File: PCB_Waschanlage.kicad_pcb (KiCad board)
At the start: 2 copper layers, 228 x 75 mm, 82 parts, among them J1 DSUB_1, J10 JMPR_LED_BTN_Sensor_1, J11 JMPR_LED_BTN_Sensor_4, J12 Conn_LED_Error, J13 Conn_LED_MainWash, J14 Conn_BTN_Start, J15 Conn_BTN_Basic, J16 Conn_LED_Motor, J17 Conn_LED_Red, J18 Conn_BTN_Sensor_1, J19 Conn_BTN_Sensor_4, J2 DSUB_2, J20 JMPR_LED_PreWash, J21 JMPR_LED_Start, J22 JMPR_LED_Basic, J23 JMPR_LED_BTN_On_Off, J24 JMPR_LED_BTN_Special, J25 JMPR_LED_Green, J26 JMPR_LED_BTN_Sensor_2, J27 JMPR_LED_BTN_Sensor_5, J28 Conn_LED_PreWash, J29 Conn_LED_Start, J3 Conn_Fuse, J30 Conn_LED_Basic, J31 Conn_BTN_On_Off, J32 Conn_BTN_Special, J33 Conn_LED_Green, J34 Conn_BTN_Sensor_2, J35 Conn_BTN_Sensor_5, J36 JMPR_LED_Special, J37 JMPR_LED_Care, J38 JMPR_LED_Underbody, J39 JMPR_LED_BTN_EmergencyOff, J4 JMPR_LED_Error, J40 JMPR_LED_BTN_Premium, J41 JMPR_LED_BTN_Sensor_3, J42 Conn_LED_Special, J43 Conn_LED_Care, J44 Conn_LED_Underbody, J45 Conn_BTN_EmergencyOff, J46 Conn_BTN_Premium, J47 Conn_BTN_Sensor_3, J48 JMPR_LED_Rims, J49 JMPR_LED_Premium, J5 JMPR_LED_MainWash, J50 JMPR_LED_Dry, J51 Conn_LED_Rims, J52 Conn_LED_Premium, J53 Conn_LED_Dry, J54 Conn_AdditionalPins_1, J55 Conn_AdditionalPins_2, J56 Conn_AdditionalPins_3, J6 JMPR_LED_BTN_Start, J7 JMPR_LED_BTN_Basic, J8 JMPR_LED_Motor, J9 JMPR_LED_Red

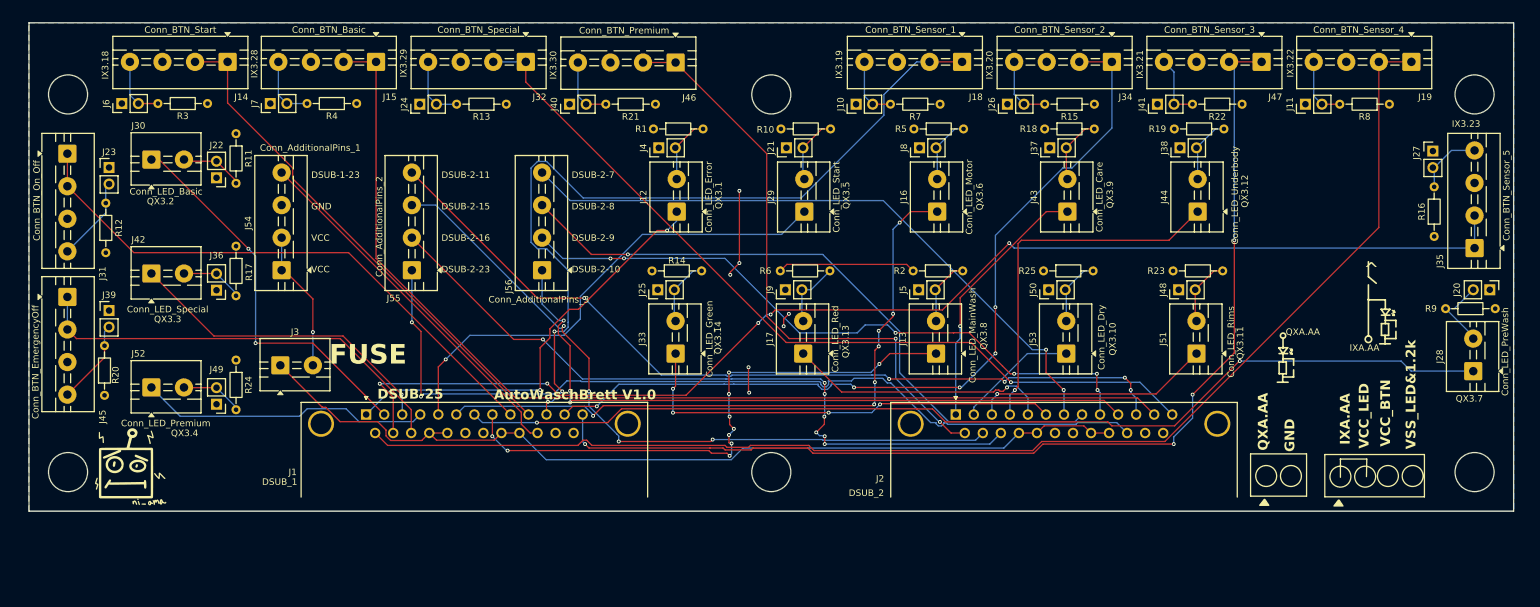
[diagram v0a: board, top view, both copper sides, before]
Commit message: Changed Connectors and Rerouting
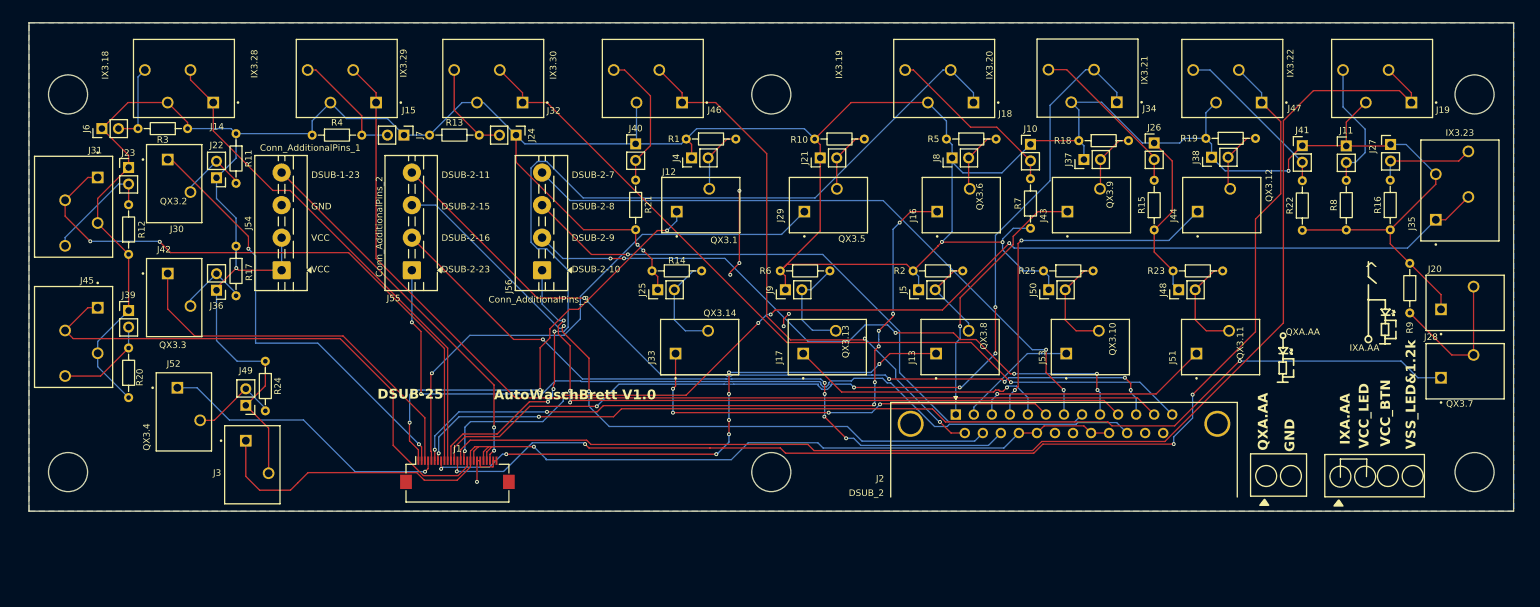
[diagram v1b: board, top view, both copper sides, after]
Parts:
- removed G***: LOGO, Doodles:robot
- J1: footprint Connector_Dsub:DSUB-25_Pins_Horizontal_P2.77x2.84mm_EdgePinOffset9.90mm_Housed_MountingHolesOffset11.32mm -> Connector_FFC-FPC:Hirose_FH12-25S-0.5SH_1x25-1MP_P0.50mm_Horizontal
- J12, J13, J16, J17, J28, J29, J3, J30, J33, J42, J43, J44, J51, J52, J53: footprint TerminalBlock:TerminalBlock_MaiXu_MX126-5.0-02P_1x02_P5.00mm -> TBL002A-350-02GY-2GY:CUI_TBL002A-350-02GY-2GY
- J14, J15, J18, J19, J31, J32, J34, J35, J45, J46, J47: footprint TerminalBlock:TerminalBlock_MaiXu_MX126-5.0-04P_1x04_P5.00mm -> TBL002A-350-04GY-2GY:CUI_TBL002A-350-04GY-2GY
- J20: footprint Connector_PinHeader_2.54mm:PinHeader_1x02_P2.54mm_Vertical -> TBL002A-350-02GY-2GY:CUI_TBL002A-350-02GY-2GY
- moved J10 27.5 mm to (194.5, 77.7), turned to 0 degrees
- moved R7 23.6 mm to (194.5, 90.6), turned to 90 degrees
- moved J26 23.3 mm to (213.5, 77.5), turned to 0 degrees
- moved J41 23.1 mm to (236.2, 77.9), turned to 0 degrees
- moved R22 21.5 mm to (236.2, 90.9), turned to 90 degrees
- moved R15 21.4 mm to (213.5, 90.8), turned to 90 degrees
- moved J7 21.1 mm to (98.3, 76.2), turned to -90 degrees
- moved R8 20.4 mm to (243.0, 90.8), turned to 90 degrees
- moved R21 19.5 mm to (133.9, 90.8), turned to 90 degrees
- moved J1 16.6 mm to (106.5, 128.1)
- moved J24 15.5 mm to (115.5, 76.2), turned to -90 degrees
- moved R9 14.9 mm to (252.8, 95.9), turned to -90 degrees
- moved J3 12.7 mm to (74.0, 123.2)
- moved R13 12.7 mm to (102.2, 76.2), turned to 0 degrees
- moved J40 11.8 mm to (133.9, 77.6), turned to 0 degrees
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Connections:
- J10 pad 1: GND -> VCC
- J11 pad 1: GND -> VCC
- J14 pad 3: GND -> VCC
- J15 pad 3: GND -> VCC
- J18 pad 3: GND -> VCC
- J19 pad 3: GND -> VCC
- J20 pad 1: GND -> VCC
- J21 pad 1: GND -> VCC
- J22 pad 1: GND -> VCC
- J23 pad 1: GND -> VCC
- J24 pad 1: GND -> VCC
- J25 pad 1: GND -> VCC
- J26 pad 1: GND -> VCC
- J27 pad 1: GND -> VCC
- J31 pad 3: GND -> VCC
- J32 pad 3: GND -> VCC
- J34 pad 3: GND -> VCC
- J35 pad 3: GND -> VCC
- J36 pad 1: GND -> VCC
- J37 pad 1: GND -> VCC
- J38 pad 1: GND -> VCC
- J39 pad 1: GND -> VCC
- J4 pad 1: GND -> VCC
- J40 pad 1: GND -> VCC
- J41 pad 1: GND -> VCC
- J45 pad 3: GND -> VCC
- J46 pad 3: GND -> VCC
- J47 pad 3: GND -> VCC
- J48 pad 1: GND -> VCC
- J49 pad 1: GND -> VCC
- J5 pad 1: GND -> VCC
- J50 pad 1: GND -> VCC
- J6 pad 1: GND -> VCC
- J7 pad 1: GND -> VCC
- J8 pad 1: GND -> VCC
- J9 pad 1: GND -> VCC
- R1 pad 1: GND -> VCC
- R10 pad 1: GND -> VCC
- R11 pad 1: GND -> VCC
- R12 pad 1: GND -> VCC
- R13 pad 1: GND -> VCC
- R14 pad 1: GND -> VCC
- R15 pad 1: GND -> VCC
- R16 pad 1: GND -> VCC
- R17 pad 1: GND -> VCC
- R18 pad 1: GND -> VCC
- R19 pad 1: GND -> VCC
- R2 pad 1: GND -> VCC
- R20 pad 1: GND -> VCC
- R21 pad 1: GND -> VCC
- R22 pad 1: GND -> VCC
- R23 pad 1: GND -> VCC
- R24 pad 1: GND -> VCC
- R25 pad 1: GND -> VCC
- R3 pad 1: GND -> VCC
- R4 pad 1: GND -> VCC
- R5 pad 1: GND -> VCC
- R6 pad 1: GND -> VCC
- R7 pad 1: GND -> VCC
- R8 pad 1: GND -> VCC
- R9 pad 1: GND -> VCC
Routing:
- net VCC: track 21.8 -> 607.8 mm, vias 1 -> 6
- net BTN_Sensor_2: track 129.4 -> 149.5 mm
- net BTN_Sensor_1: track 124.1 -> 143.0 mm
- net Net-(J10-Pin_2): track 9.76 -> 27.8 mm
- net BTN_Sensor_3: track 164.4 -> 181.8 mm
- net BTN_EmergencyOff: track 66.5 -> 83.7 mm
- net GND: track 41.1 -> 24.0 mm, vias 7 -> 6
- net BTN_Sensor_5: track 192.3 -> 175.4 mm
- net Net-(J41-Pin_2): track 9.98 -> 25.5 mm
- net Net-(J26-Pin_2): track 10.3 -> 25.4 mm
- net VCC_in: track 140.7 -> 155.7 mm, vias 0 -> 1
- net Net-(J20-Pin_2): track 11.8 -> 23.1 mm
- net Net-(J40-Pin_2): track 9.95 -> 21.2 mm
- net Net-(J11-Pin_2): track 9.76 -> 20.4 mm
- net LED_Special: track 49.2 -> 58.5 mm, vias 1 -> 0
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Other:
- board text removed: "FUSE"

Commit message: Added new connectors on the PCB
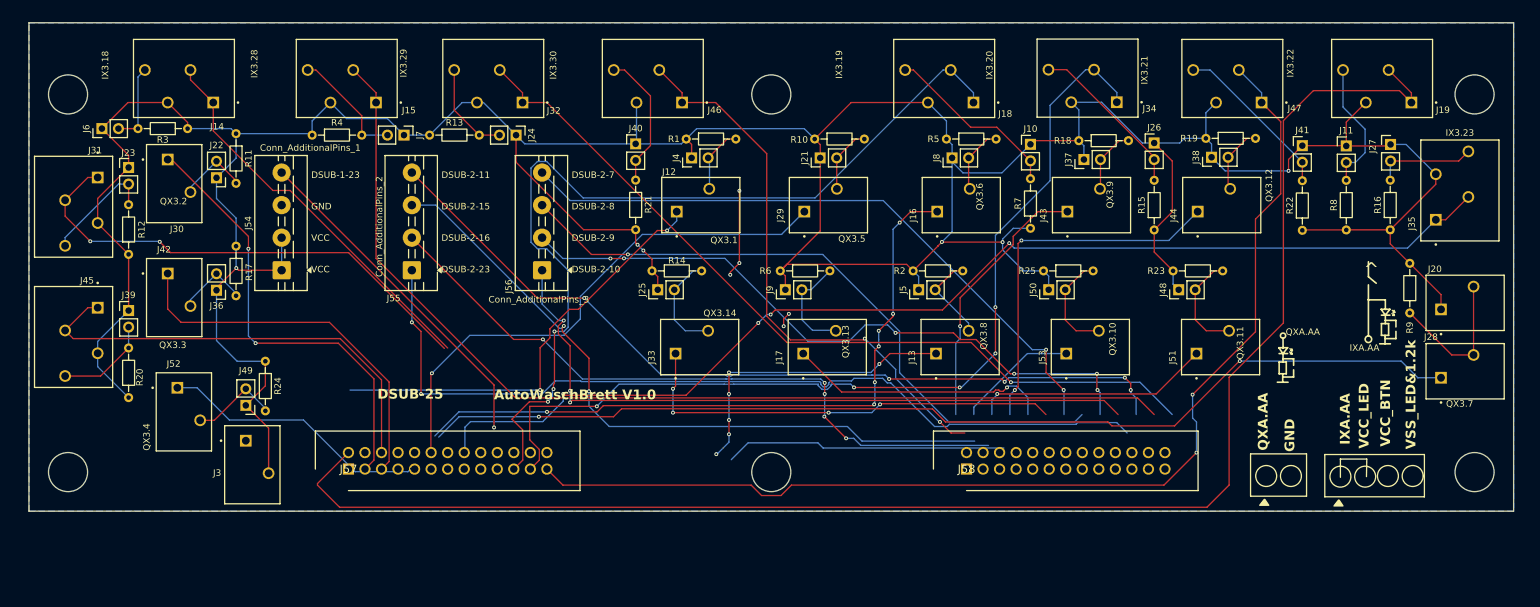
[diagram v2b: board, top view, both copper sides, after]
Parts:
- removed J1: DSUB_1, Connector_FFC-FPC:Hirose_FH12-25S-0.5SH_1x25-1MP_P0.50mm_Horizontal
- removed J2: DSUB_2, Connector_Dsub:DSUB-25_Pins_Horizontal_P2.77x2.84mm_EdgePinOffset9.90mm_Housed_MountingHolesOffset11.32mm
- added J57: 5103308-6, project:SHDR26W66P254_2X13_4051X914X986P, F.Cu at (89.8, 127.5)
- added J58: 5103308-6, project:SHDR26W66P254_2X13_4051X914X986P, F.Cu at (184.7, 127.5)
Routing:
- net VCC_in: track 155.7 -> 43.3 mm, vias 1 -> 0
- net LED_MainWash: track 90.9 -> 46.5 mm, vias 8 -> 6
- net BTN_Sensor_4: track 197.3 -> 238.0 mm
- net BTN_Start: track 77.9 -> 60.6 mm
- net BTN_ON_OFF: track 92.8 -> 75.6 mm
- net BTN_EmergencyOff: track 83.7 -> 69.3 mm
- net BTN_Sensor_3: track 181.8 -> 171.5 mm, vias 4 -> 2
- net GND: track 24.0 -> 15.9 mm, vias 6 -> 5
- net BTN_Sensor_2: track 149.5 -> 144.1 mm
- net DSUB_1_PIN_23: track 58.1 -> 52.7 mm, vias 2 -> 1
- net BTN_Sensor_1: track 143.0 -> 138.6 mm
- net LED_Premium: track 45.3 -> 41.4 mm
- net LED_Motor: track 109.3 -> 105.5 mm, vias 8 -> 7
- net LED_PreWash: track 165.7 -> 162.0 mm, vias 3 -> 2
- net DSUB_2_PIN_16: track 107.6 -> 104.9 mm
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
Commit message: Routing fimished
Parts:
- J54, J55, J56: footprint TerminalBlock:TerminalBlock_MaiXu_MX126-5.0-04P_1x04_P5.00mm -> TBL002A-350-04GY-2GY:CUI_TBL002A-350-04GY-2GY
- moved J54 13.3 mm to (92.1, 92.6), turned to 180 degrees
- moved J55 11.3 mm to (109.9, 92.6), turned to 180 degrees
- moved J56 9.31 mm to (127.7, 92.6), turned to 180 degrees
- moved J3 5.89 mm to (72.2, 117.5)
- moved J49 5.39 mm to (72.0, 112.8)
- moved R24 5.01 mm to (75.5, 106.2)
- moved J58 3.02 mm to (184.3, 124.5)
- moved J57 3.00 mm to (89.8, 124.5)
- moved J52 2.50 mm to (62.5, 112.8)
- moved J40 2.40 mm to (136.0, 76.5)
- moved R14 1.79 mm to (134.6, 97.2)
- moved J25 1.79 mm to (135.5, 100.1)
- moved R21 1.13 mm to (135.0, 90.8)
- moved R15 0.75 mm to (214.2, 90.8)
- moved J10 0.54 mm to (194.0, 77.5)
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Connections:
- J55 pad 4: DSUB_2_PIN_11 -> DSUB_2_PIN_10
- J56 pad 1: DSUB_2_PIN_10 -> DSUB_2_PIN_11
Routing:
- net VCC_in: track 43.3 -> 220.8 mm, vias 0 -> 2
- net GND: track 15.9 -> 114.0 mm, vias 5 -> 26
- net VCC: track 607.8 -> 691.8 mm, vias 6 -> 0
- net BTN_Sensor_5: track 174.1 -> 244.6 mm, vias 5 -> 1
- net LED_Care: track 40.9 -> 96.6 mm, vias 1 -> 2
- net LED_Basic: track 69.5 -> 119.1 mm, vias 2 -> 0
- net LED_MainWash: track 46.5 -> 92.6 mm, vias 6 -> 1
- net BTN_Sensor_2: track 144.1 -> 189.7 mm, vias 5 -> 0
- net DSUB_2_PIN_9: track 102.4 -> 135.9 mm, vias 6 -> 2
- net DSUB_2_PIN_10: track 108.4 -> 139.2 mm, vias 3 -> 0
- net LED_Underbody: track 56.4 -> 78.9 mm, vias 2 -> 1
- net BTN_Basic: track 159.8 -> 182.0 mm
- net BTN_Start: track 60.6 -> 81.8 mm
- net DSUB_2_PIN_7: track 99.8 -> 120.9 mm, vias 2 -> 1
- net BTN_Sensor_4: track 238.0 -> 258.7 mm
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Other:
- board text added: "DSUB-1-23"
- board text added: "DSUB-2-10"
- board text added: "DSUB-2-11"
- board text added: "DSUB-2-15"
- board text added: "DSUB-2-16"
- board text added: "DSUB-2-23"
- board text added: "DSUB-2-7"
- board text added: "DSUB-2-8"
- board text added: "DSUB-2-9"
- board text added: "LED ???"
- board text added: "LED motor"
- board text added: "LED start"
- board text added: "Spare I/O"
- board text added: "VCC"
- board text added: "basic button"
- board text added: "premium button"
- board text added: "special button"
- board text added: "start button"
- board text removed: "DSUB-1-23 GND VCC VCC"
- board text removed: "DSUB-2-11 DSUB-2-15 DSUB-2-16 DSUB-2-23"
- board text removed: "DSUB-2-7 DSUB-2-8 DSUB-2-9 DSUB-2-10"
- board text removed: "^"

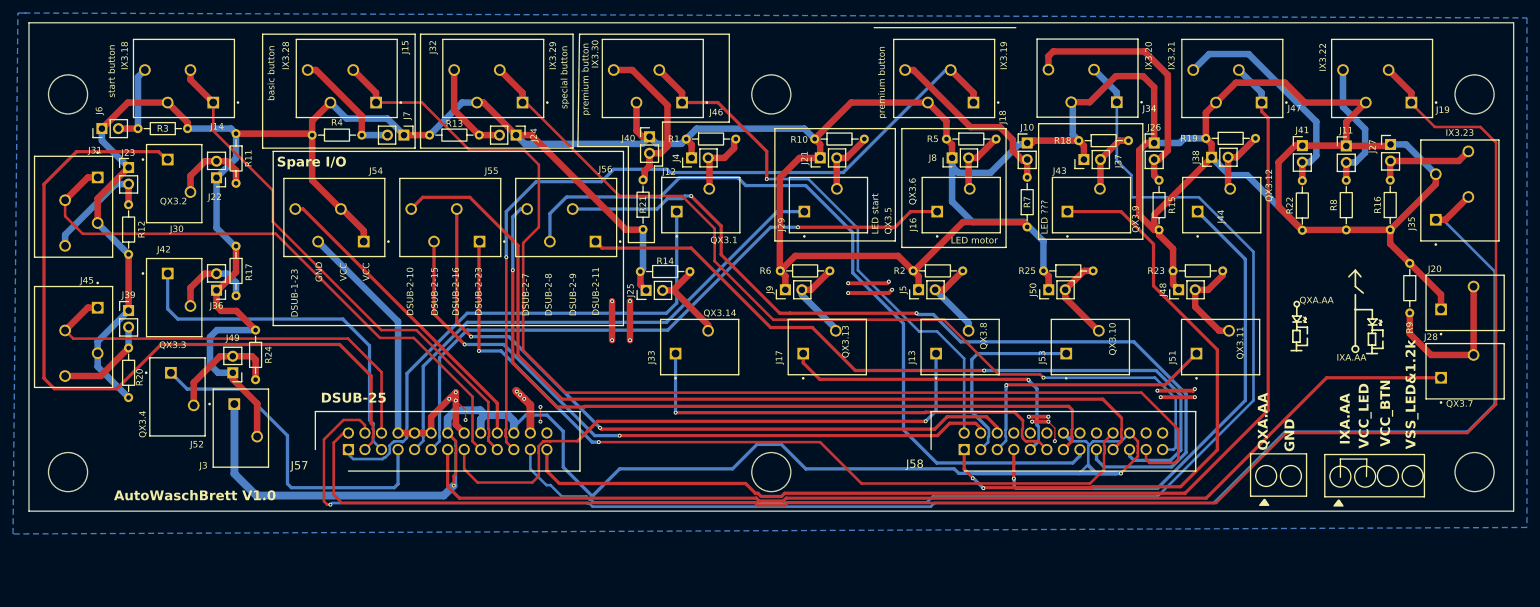
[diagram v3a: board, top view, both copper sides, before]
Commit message: Silkscreen added
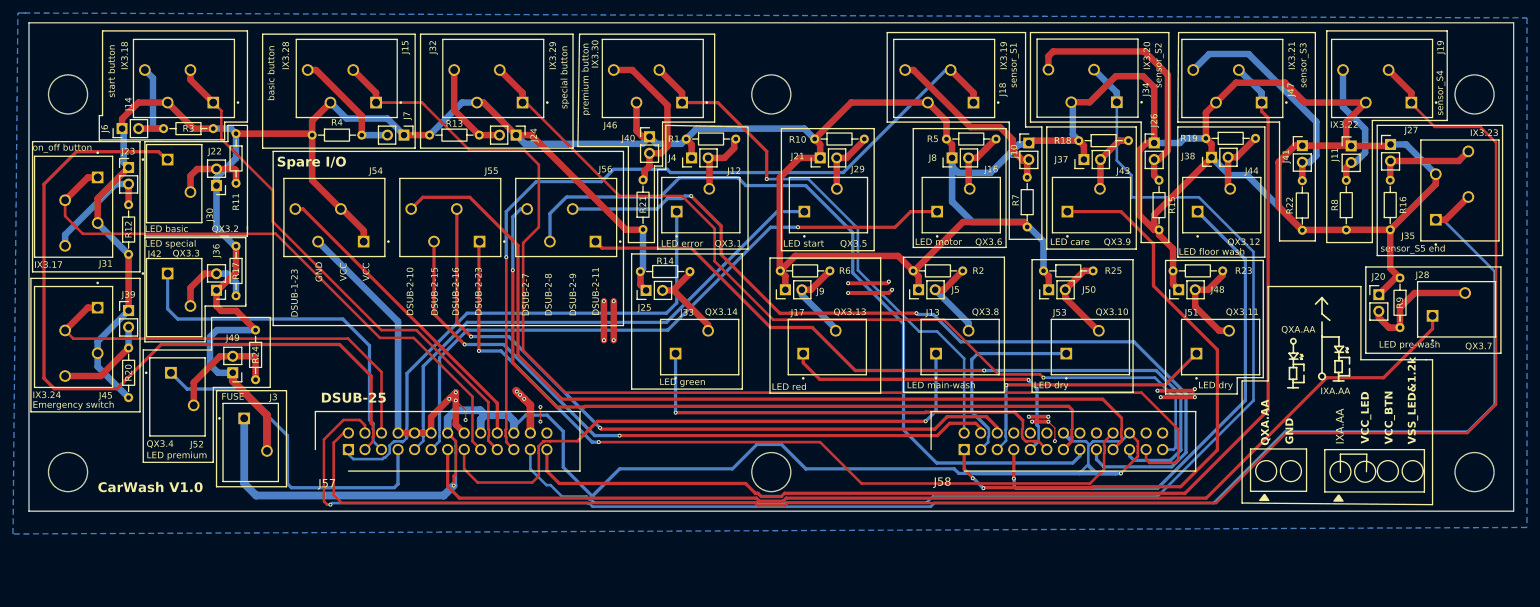
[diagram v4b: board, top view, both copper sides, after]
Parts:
- J20: footprint TBL002A-350-02GY-2GY:CUI_TBL002A-350-02GY-2GY -> Connector_PinHeader_2.54mm:PinHeader_1x02_P2.54mm_Vertical
- moved J20 9.81 mm to (248.0, 100.8), turned to 0 degrees
- moved J28 9.60 mm to (256.2, 104.0)
- moved R3 3.94 mm to (69.0, 75.2)
- moved J6 3.10 mm to (55.0, 75.2)
- moved R9 2.70 mm to (251.2, 98.2)
- moved J3 2.67 mm to (73.8, 119.8)
- moved J22 1.20 mm to (69.5, 84.0)
- moved J11 0.75 mm to (243.8, 77.9)
- moved J10 0.25 mm to (194.2, 77.5)
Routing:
- net Net-(J20-Pin_2): track 24.9 -> 18.9 mm
- net VCC: track 691.8 -> 687.7 mm
- net LED_PreWash: track 167.0 -> 170.8 mm
- net VCC_in: track 220.8 -> 218.0 mm
- net Net-(J14-Pin_4): track 12.4 -> 14.9 mm
- net Net-(J22-Pin_2): track 13.0 -> 12.0 mm
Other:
- board text added: "CarWash V1.0"
- board text added: "Emergency switch"
- board text added: "FUSE"
- board text added: "IX3.17"
- board text added: "IX3.24"
- board text added: "LED basic"
- board text added: "LED care"
- board text added: "LED dry"
- board text added: "LED error"
- board text added: "LED floor wash"
- board text added: "LED green"
- board text added: "LED main-wash"
- board text added: "LED pre-wash"
- board text added: "LED premium"
- board text added: "LED red"
- board text added: "LED special"
- board text added: "on_off button"
- board text added: "sensor_S1"
- board text added: "sensor_S2"
- board text added: "sensor_S3"
- board text added: "sensor_S4"
- board text added: "sensor_S5 end"
- board text removed: "AutoWaschBrett V1.0"
- board text removed: "LED ???"

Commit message: added text ToDos
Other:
- board text added: "To Do: - d-sub beschriftn - name und github repo und qr - ID symbol - Kontrolle Maße - Stückliste"
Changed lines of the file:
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@@
+		)
+	)
+	(gr_text "To Do:\n- d-sub beschriftn\n- name und github repo und qr\n- ID symbol\n- Kontrolle Maße\n- Stückliste\n"
+		(at 40.75 146.25 0)
+		(layer "F.SilkS")
+		(effects
+			(font
+				(size 1 1)
+				(thickness 0.15)
+			)
+			(justify left bottom)
 		)
 	)

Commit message: Design finished. open: only review
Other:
- board text added: "DSUB-25-1"
- board text added: "DSUB-25-2"
- board text added: "PLA 05.2026 Felix Mäher"
- board text added: "To Do: - Kontrolle Maße (Stecker, Bohrung) - Stückliste"
- board text added: "github.com/Planky0815"
- board text removed: "DSUB-25"
- board text removed: "To Do: - d-sub beschriftn - name und github repo und qr - ID symbol - Kontrolle Maße - Stückliste"

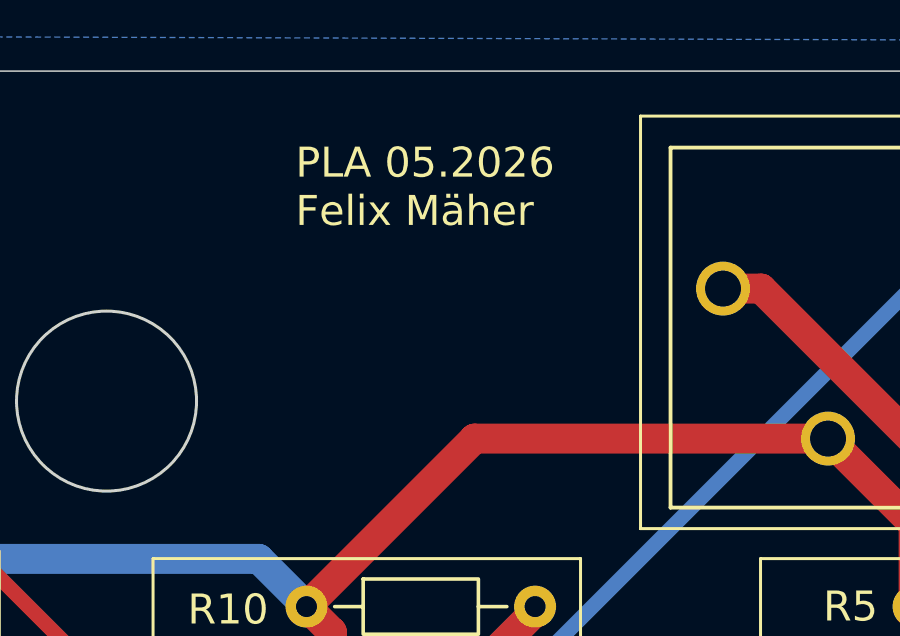
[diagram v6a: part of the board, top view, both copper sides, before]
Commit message: Added Datasheet, Created BOM, Included Links to Connectors
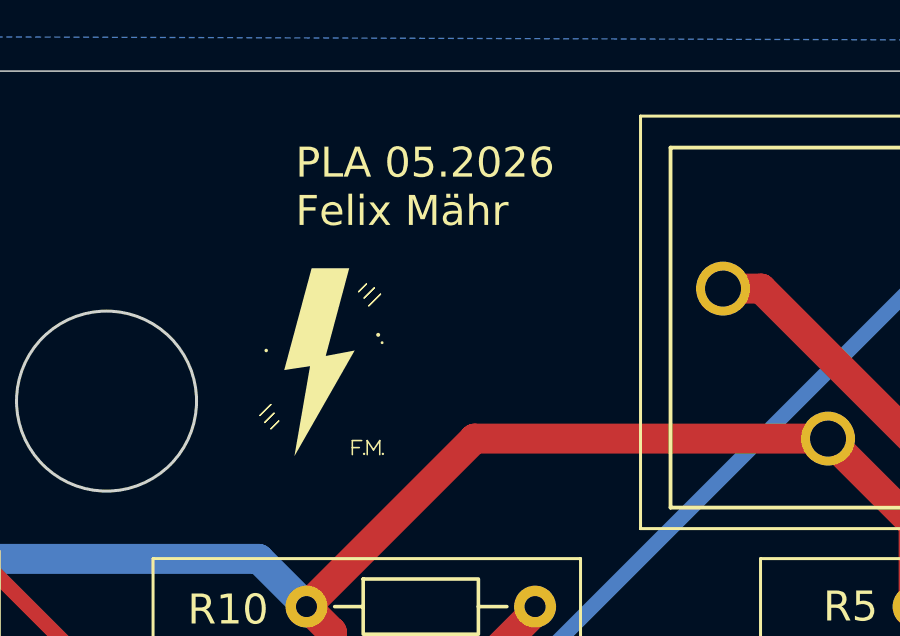
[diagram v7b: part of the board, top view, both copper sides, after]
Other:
- board text added: "PLA 05.2026 Felix Mähr"
- board text removed: "PLA 05.2026 Felix Mäher"

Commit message: Bug fixes
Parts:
- moved J6 1.35 mm to (53.8, 75.8)
- moved R11 0.50 mm to (73.0, 76.0)
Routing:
- net VCC: track 687.7 -> 689.5 mm
- net Net-(J14-Pin_4): track 14.9 -> 16.4 mm
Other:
- board text added: "Felix Mähr"
- board text added: "PLA 05.2026"
- board text removed: "PLA 05.2026 Felix Mähr"
